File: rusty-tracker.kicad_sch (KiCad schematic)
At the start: 176 parts, among them J1 SIM8051-6-0-14-01-X, J2 USB_C_Receptacle_USB2.0, J3 NFC, J4 tag-connect-swd, J5 Battery Connector, J6 Conn_01x01, J7 Conn_01x01, Q1 RUM002N02T2L, Q2 RUM002N02T2L, Q3 RUM002N02T2L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

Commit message: Order sent to JLCPCB
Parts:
- J3: footprint Connector_JST:JST_SH_SM02B-SRSS-TB_1x02-1MP_P1.00mm_Horizontal -> Connector_FFC-FPC:TE_0-1734839-5_1x05-1MP_P0.5mm_Horizontal; symbol Connector_Generic_MountingPin:Conn_01x02_MountingPin -> Connector_Generic_MountingPin:Conn_01x05_MountingPin
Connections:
- net NFC1: now also J3.2 (Pin_2); no longer J3.1 (Pin_1)
- net NFC2: now also J3.4 (Pin_4); no longer J3.2 (Pin_2)
- no-connect marks 57 -> 60
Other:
- moved on the sheet: C17, C20
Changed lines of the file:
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@@
   (junction (at 190.5 177.8) (diameter 0) (color 0 0 0 0)
   )
-  (junction (at 382.27 121.92) (diameter 0) (color 0 0 0 0)
+  (junction (at 383.54 119.38) (diameter 0) (color 0 0 0 0)
   )
   (junction (at 280.67 72.39) (diameter 0) (color 0 0 0 0)
@@
   (junction (at 173.99 165.1) (diameter 0) (color 0 0 0 0)
   )
-  (junction (at 382.27 124.46) (diameter 0) (color 0 0 0 0)
+  (junction (at 383.54 124.46) (diameter 0) (color 0 0 0 0)
   )
   (junction (at 173.99 222.25) (diameter 0) (color 0 0 0 0)
@@
   (no_connect (at 107.95 91.44))
   (no_connect (at 353.06 165.1))
+  (no_connect (at 386.08 121.92))
   (no_connect (at 142.24 252.73))
   (no_connect (at 50.8 227.33))
@@
   (no_connect (at 107.95 60.96))
   (no_connect (at 142.24 250.19))
+  (no_connect (at 386.08 116.84))
   (no_connect (at 68.58 227.33))
   (no_connect (at 287.02 205.74))
@@
   (no_connect (at 77.47 227.33))
   (no_connect (at 107.95 58.42))
+  (no_connect (at 386.08 127))
   (no_connect (at 64.77 62.23))
   (no_connect (at 24.13 227.33))
@@
     (stroke (width 0) (type default))
   )
-  (wire (pts (xy 382.27 124.46) (xy 382.27 127))
+  (wire (pts (xy 383.54 124.46) (xy 383.54 127))
     (stroke (width 0) (type default))
   )
@@
     (stroke (width 0) (type default))
   )
-  (wire (pts (xy 382.27 119.38) (xy 382.27 121.92))
+  (wire (pts (xy 383.54 116.84) (xy 383.54 119.38))
     (stroke (width 0) (type default))
   )
@@
     (stroke (width 0) (type default))
   )
-  (wire (pts (xy 378.46 124.46) (xy 382.27 124.46))
+  (wire (pts (xy 379.73 124.46) (xy 383.54 124.46))
     (stroke (width 0) (type default))
   )
@@
     (stroke (width 0) (type default))
   )
-  (wire (pts (xy 378.46 121.92) (xy 382.27 121.92))
+  (wire (pts (xy 379.73 119.38) (xy 383.54 119.38))
     (stroke (width 0) (type default))
   )
@@
     (stroke (width 0.3) (type default))
   )
-  (wire (pts (xy 382.27 121.92) (xy 384.81 121.92))
+  (wire (pts (xy 383.54 119.38) (xy 386.08 119.38))
     (stroke (width 0) (type default))
   )
@@
     (stroke (width 0) (type default))
   )
-  (wire (pts (xy 382.27 124.46) (xy 384.81 124.46))
+  (wire (pts (xy 383.54 124.46) (xy 386.08 124.46))
     (stroke (width 0) (type default))
   )
@@
     (effects (font (size 1.27 1.27)) (justify left bottom))
   )
-  (label "NFC1" (at 378.46 124.46 180) (fields_autoplaced)
+  (label "NFC1" (at 379.73 124.46 180) (fields_autoplaced)
     (effects (font (size 1.27 1.27)) (justify right bottom))
   )
@@
     (effects (font (size 1.27 1.27)) (justify right bottom))
   )
-  (label "NFC2" (at 378.46 121.92 180) (fields_autoplaced)
+  (label "NFC2" (at 379.73 119.38 180) (fields_autoplaced)
     (effects (font (size 1.27 1.27)) (justify right bottom))
   )
@@
     )
   )
-  (symbol (lib_id "power:GND") (at 382.27 114.3 0) (mirror x) (unit 1)
+  (symbol (lib_id "power:GND") (at 383.54 111.76 0) (mirror x) (unit 1)
     (in_bom yes) (on_board yes) (dnp no)
-    (property "Reference" "#PWR055" (at 382.27 107.95 0)
+    (property "Reference" "#PWR055" (at 383.54 105.41 0)
       (effects (font (size 1.27 1.27)) hide)
     )
-    (property "Value" "GND" (at 382.397 111.0488 90)
+    (property "Value" "GND" (at 383.667 108.5088 90)
       (effects (font (size 1.27 1.27)) (justify right) hide)
     )
-    (property "Footprint" "" (at 382.27 114.3 0)
+    (property "Footprint" "" (at 383.54 111.76 0)
       (effects (font (size 1.27 1.27)))
     )
-    (property "Datasheet" "" (at 382.27 114.3 0)
+    (property "Datasheet" "" (at 383.54 111.76 0)
       (effects (font (size 1.27 1.27)))
     )
@@
     )
   )
-  (symbol (lib_id "Device:C_Small") (at 382.27 129.54 0) (mirror y) (unit 1)
-    (in_bom yes) (on_board yes) (dnp no)
-    (property "Reference" "C20" (at 384.6068 130.7084 0)
-      (effects (font (size 1.27 1.27)) (justify right))
+  (symbol (lib_id "Device:C_Small") (at 383.54 129.54 0) (mirror y) (unit 1)
+    (in_bom yes) (on_board yes) (dnp no) (fields_autoplaced)
+    (property "Reference" "C20" (at 381 128.9113 0)
+      (effects (font (size 1.27 1.27)) (justify left))
     )
-    (property "Value" "DNP" (at 384.6068 128.397 0)
-      (effects (font (size 1.27 1.27)) (justify right))
+    (property "Value" "DNP" (at 381 131.4513 0)
+      (effects (font (size 1.27 1.27)) (justify left))
     )
-    (property "Footprint" "passive:C_0402" (at 382.27 129.54 0)
+    (property "Footprint" "passive:C_0402" (at 383.54 129.54 0)
       (effects (font (size 1.27 1.27)) hide)
     )
-    (property "Datasheet" "" (at 382.27 129.54 0)
+    (property "Datasheet" "" (at 383.54 129.54 0)
       (effects (font (size 1.27 1.27)))
     )
-    (property "Tolerance" "" (at 382.27 129.54 0)
+    (property "Tolerance" "" (at 383.54 129.54 0)
       (effects (font (size 1.524 1.524)) hide)
     )
-    (property "Manufacturer" "" (at 528.32 309.88 0)
+    (property "Manufacturer" "" (at 529.59 309.88 0)
       (effects (font (size 1.524 1.524)) hide)
     )
-    (property "MFPN" "" (at 382.27 129.54 0)
+    (property "MFPN" "" (at 383.54 129.54 0)
       (effects (font (size 1.27 1.27)) hide)
     )
-    (property "Comment" "C0G,50V" (at 382.27 129.54 0)
+    (property "Comment" "C0G,50V" (at 383.54 129.54 0)
       (effects (font (size 1.27 1.27)) hide)
     )
@@
     )
   )
-  (symbol (lib_id "power:GND") (at 382.27 132.08 0) (mirror y) (unit 1)
+  (symbol (lib_id "power:GND") (at 383.54 132.08 0) (mirror y) (unit 1)
     (in_bom yes) (on_board yes) (dnp no)
-    (property "Reference" "#PWR059" (at 382.27 138.43 0)
+    (property "Reference" "#PWR059" (at 383.54 138.43 0)
       (effects (font (size 1.27 1.27)) hide)
     )
-    (property "Value" "GND" (at 382.143 135.3312 90)
+    (property "Value" "GND" (at 383.413 135.3312 90)
       (effects (font (size 1.27 1.27)) (justify right) hide)
     )
-    (property "Footprint" "" (at 382.27 132.08 0)
+    (property "Footprint" "" (at 383.54 132.08 0)
       (effects (font (size 1.27 1.27)))
     )
-    (property "Datasheet" "" (at 382.27 132.08 0)
+    (property "Datasheet" "" (at 383.54 132.08 0)
       (effects (font (size 1.27 1.27)))
     )
@@
     )
   )
-  (symbol (lib_id "power:GND") (at 389.89 116.84 180) (unit 1)
+  (symbol (lib_id "power:GND") (at 391.16 111.76 180) (unit 1)
     (in_bom yes) (on_board yes) (dnp no) (fields_autoplaced)
-    (property "Reference" "#PWR061" (at 389.89 110.49 0)
+    (property "Reference" "#PWR061" (at 391.16 105.41 0)
       (effects (font (size 1.27 1.27)) hide)
     )
-    (property "Value" "GND" (at 389.763 113.5888 90)
+    (property "Value" "GND" (at 391.033 108.5088 90)
       (effects (font (size 1.27 1.27)) (justify right) hide)
     )
-    (property "Footprint" "" (at 389.89 116.84 0)
+    (property "Footprint" "" (at 391.16 111.76 0)
       (effects (font (size 1.27 1.27)) hide)
     )
-    (property "Datasheet" "" (at 389.89 116.84 0)
+    (property "Datasheet" "" (at 391.16 111.76 0)
       (effects (font (size 1.27 1.27)) hide)
     )
@@
     )
   )
-  (symbol (lib_id "Device:C_Small") (at 382.27 116.84 0) (mirror x) (unit 1)
-    (in_bom yes) (on_board yes) (dnp no)
-    (property "Reference" "C17" (at 379.9332 115.6716 0)
+  (symbol (lib_id "Device:C_Small") (at 383.54 114.3 0) (mirror x) (unit 1)
+    (in_bom yes) (on_board yes) (dnp no) (fields_autoplaced)
+    (property "Reference" "C17" (at 381 113.6586 0)
       (effects (font (size 1.27 1.27)) (justify right))
     )
-    (property "Value" "DNP" (at 379.9332 117.983 0)
+    (property "Value" "DNP" (at 381 116.1986 0)
       (effects (font (size 1.27 1.27)) (justify right))
     )
-    (property "Footprint" "passive:C_0402" (at 382.27 116.84 0)
+    (property "Footprint" "passive:C_0402" (at 383.54 114.3 0)
       (effects (font (size 1.27 1.27)) hide)
     )
-    (property "Datasheet" "" (at 382.27 116.84 0)
+    (property "Datasheet" "" (at 383.54 114.3 0)
       (effects (font (size 1.27 1.27)))
     )
-    (property "Tolerance" "" (at 382.27 116.84 0)
+    (property "Tolerance" "" (at 383.54 114.3 0)
       (effects (font (size 1.524 1.524)) hide)
     )
-    (property "Manufacturer" "" (at 236.22 -63.5 0)
+    (property "Manufacturer" "" (at 237.49 -66.04 0)
       (effects (font (size 1.524 1.524)) hide)
     )
-    (property "MFPN" "" (at 382.27 116.84 0)
+    (property "MFPN" "" (at 383.54 114.3 0)
       (effects (font (size 1.27 1.27)) hide)
     )
-    (property "Comment" "C0G,50V" (at 382.27 116.84 0)
+    (property "Comment" "C0G,50V" (at 383.54 114.3 0)
       (effects (font (size 1.27 1.27)) hide)
     )
@@
     )
   )
-  (symbol (lib_id "Connector_Generic_MountingPin:Conn_01x02_MountingPin") (at 389.89 124.46 0) (mirror x) (unit 1)
+  (symbol (lib_id "Connector_Generic_MountingPin:Conn_01x05_MountingPin") (at 391.16 121.92 0) (mirror x) (unit 1)
     (in_bom yes) (on_board yes) (dnp no) (fields_autoplaced)
-    (property "Reference" "J3" (at 392.43 121.5643 0)
+    (property "Reference" "J3" (at 393.7 119.0243 0)
       (effects (font (size 1.27 1.27)) (justify left))
     )
-    (property "Value" "NFC" (at 392.43 124.1043 0)
+    (property "Value" "NFC" (at 393.7 121.5643 0)
       (effects (font (size 1.27 1.27)) (justify left))
     )
-    (property "Footprint" "Connector_JST:JST_SH_SM02B-SRSS-TB_1x02-1MP_P1.00mm_Horizontal" (at 389.89 124.46 0)
+    (property "Footprint" "Connector_FFC-FPC:TE_0-1734839-5_1x05-1MP_P0.5mm_Horizontal" (at 391.16 121.92 0)
       (effects (font (size 1.27 1.27)) hide)
     )
-    (property "Datasheet" "~" (at 389.89 124.46 0)
+    (property "Datasheet" "~" (at 391.16 121.92 0)
       (effects (font (size 1.27 1.27)) hide)
     )
-    (property "MFPN" "SM02B-SRSS-TB(LF)(SN)" (at 389.89 124.46 0)
+    (property "MFPN" "SM02B-SRSS-TB(LF)(SN)" (at 391.16 121.92 0)
       (effects (font (size 1.27 1.27)) hide)
     )
     (pin "1")
     (pin "2")
+    (pin "3")
+    (pin "4")
+    (pin "5")
     (pin "MP")
     (instances

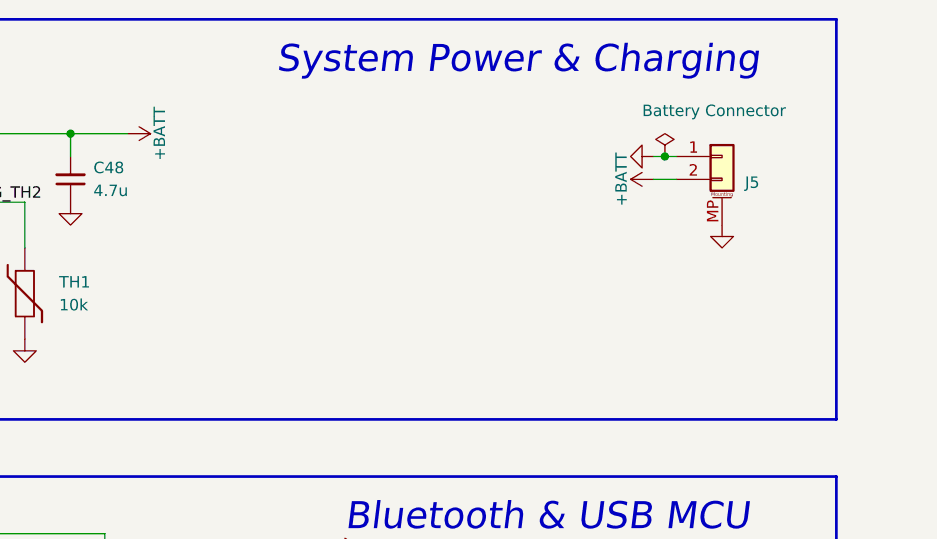
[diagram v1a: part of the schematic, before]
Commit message: Add an exported schematic so people don't need to download and check
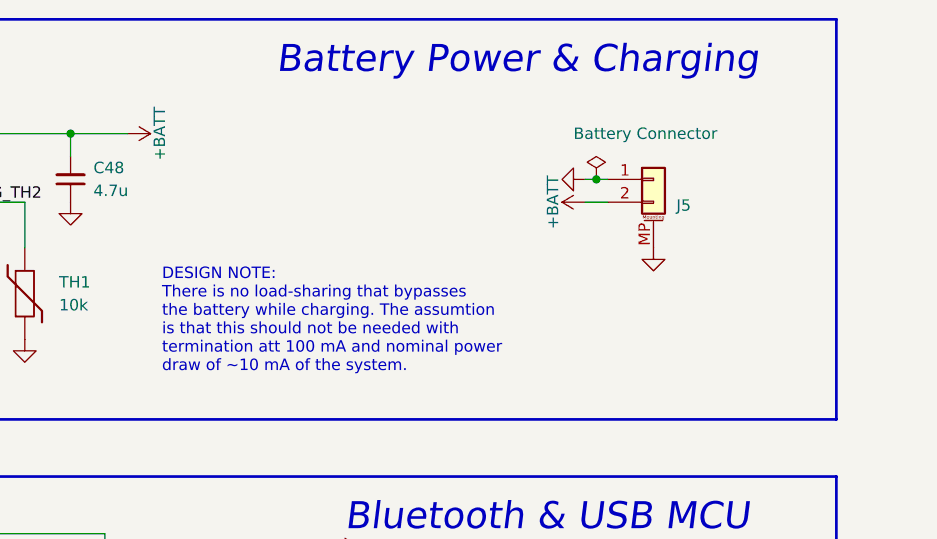
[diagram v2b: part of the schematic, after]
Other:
- note added: "Battery Power & Charging"
- note added: "DESIGN NOTE: There is no load-sharing that bypasses the battery while charging. The assumtion is that this should not be needed with termination att 100 mA and nominal power draw of ~10 mA of the system."
- note removed: "System Power & Charging"
- moved on the sheet: J5
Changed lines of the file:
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@@
   (junction (at 58.42 133.35) (diameter 0) (color 0 0 0 0)
   )
-  (junction (at 382.27 30.48) (diameter 0) (color 0 0 0 0)
+  (junction (at 374.65 33.02) (diameter 0) (color 0 0 0 0)
   )
   (junction (at 381 226.06) (diameter 0) (color 0 0 0 0)
@@
     (stroke (width 0.3) (type default))
   )
-  (wire (pts (xy 382.27 30.48) (xy 383.54 30.48))
+  (wire (pts (xy 374.65 33.02) (xy 375.92 33.02))
     (stroke (width 0) (type default))
   )
@@
     (stroke (width 0) (type default))
   )
-  (wire (pts (xy 381 33.02) (xy 383.54 33.02))
+  (wire (pts (xy 373.38 35.56) (xy 375.92 35.56))
     (stroke (width 0) (type default))
   )
@@
     (stroke (width 0) (type default))
   )
-  (wire (pts (xy 381 30.48) (xy 382.27 30.48))
+  (wire (pts (xy 373.38 33.02) (xy 374.65 33.02))
     (stroke (width 0) (type default))
   )
@@
     (effects (font (size 2 2) italic) (justify right bottom))
   )
-  (text "System Power & Charging" (at 339.09 21.59 0)
+  (text "Battery Power & Charging" (at 339.09 21.59 0)
     (effects (font (size 3 3) italic) (justify left bottom))
   )
@@
     (effects (font (size 2 2) italic) (justify right bottom))
   )
+  (text "DESIGN NOTE:\nThere is no load-sharing that bypasses \nthe battery while charging. The assumtion \nis that this should not be needed with \ntermination att 100 mA and nominal power \ndraw of ~10 mA of the system."
+    (at 326.39 54.61 0)
+    (effects (font (size 1.27 1.27)) (justify left bottom))
+  )
   (label "DEC4_6" (at 312.42 91.44 90) (fields_autoplaced)
     (effects (font (size 1.27 1.27)) (justify left bottom))
@@
     )
   )
-  (symbol (lib_id "power:PWR_FLAG") (at 382.27 30.48 0) (mirror y) (unit 1)
+  (symbol (lib_id "power:PWR_FLAG") (at 374.65 33.02 0) (mirror y) (unit 1)
     (in_bom yes) (on_board yes) (dnp no) (fields_autoplaced)
-    (property "Reference" "#FLG0102" (at 382.27 28.575 0)
+    (property "Reference" "#FLG0102" (at 374.65 31.115 0)
       (effects (font (size 1.27 1.27)) hide)
     )
-    (property "Value" "PWR_FLAG" (at 382.27 25.4 0)
+    (property "Value" "PWR_FLAG" (at 374.65 27.94 0)
       (effects (font (size 1.27 1.27)) hide)
     )
-    (property "Footprint" "" (at 382.27 30.48 0)
+    (property "Footprint" "" (at 374.65 33.02 0)
       (effects (font (size 1.27 1.27)) hide)
     )
-    (property "Datasheet" "~" (at 382.27 30.48 0)
+    (property "Datasheet" "~" (at 374.65 33.02 0)
       (effects (font (size 1.27 1.27)) hide)
     )
@@
     )
   )
-  (symbol (lib_id "power:GND") (at 381 30.48 270) (mirror x) (unit 1)
+  (symbol (lib_id "power:GND") (at 373.38 33.02 270) (mirror x) (unit 1)
     (in_bom yes) (on_board yes) (dnp no) (fields_autoplaced)
-    (property "Reference" "#PWR056" (at 374.65 30.48 0)
+    (property "Reference" "#PWR056" (at 367.03 33.02 0)
       (effects (font (size 1.27 1.27)) hide)
     )
-    (property "Value" "GND" (at 377.7488 30.353 90)
+    (property "Value" "GND" (at 370.1288 32.893 90)
       (effects (font (size 1.27 1.27)) (justify right) hide)
     )
-    (property "Footprint" "" (at 381 30.48 0)
+    (property "Footprint" "" (at 373.38 33.02 0)
       (effects (font (size 1.27 1.27)) hide)
     )
-    (property "Datasheet" "" (at 381 30.48 0)
+    (property "Datasheet" "" (at 373.38 33.02 0)
       (effects (font (size 1.27 1.27)) hide)
     )
@@
     )
   )
-  (symbol (lib_id "power:+BATT") (at 381 33.02 90) (mirror x) (unit 1)
+  (symbol (lib_id "power:+BATT") (at 373.38 35.56 90) (mirror x) (unit 1)
     (in_bom yes) (on_board yes) (dnp no) (fields_autoplaced)
-    (property "Reference" "#PWR0142" (at 384.81 33.02 0)
+    (property "Reference" "#PWR0142" (at 377.19 35.56 0)
       (effects (font (size 1.27 1.27)) hide)
     )
-    (property "Value" "+BATT" (at 377.444 33.02 0)
+    (property "Value" "+BATT" (at 369.824 35.56 0)
       (effects (font (size 1.27 1.27)))
     )
-    (property "Footprint" "" (at 381 33.02 0)
+    (property "Footprint" "" (at 373.38 35.56 0)
       (effects (font (size 1.27 1.27)) hide)
     )
-    (property "Datasheet" "" (at 381 33.02 0)
+    (property "Datasheet" "" (at 373.38 35.56 0)
       (effects (font (size 1.27 1.27)) hide)
     )
@@
     )
   )
-  (symbol (lib_id "Connector_Generic_MountingPin:Conn_01x02_MountingPin") (at 388.62 30.48 0) (unit 1)
+  (symbol (lib_id "Connector_Generic_MountingPin:Conn_01x02_MountingPin") (at 381 33.02 0) (unit 1)
     (in_bom yes) (on_board yes) (dnp no)
-    (property "Reference" "J5" (at 391.16 33.3757 0)
+    (property "Reference" "J5" (at 383.54 35.9157 0)
       (effects (font (size 1.27 1.27)) (justify left))
     )
-    (property "Value" "Battery Connector" (at 379.73 25.4 0)
+    (property "Value" "Battery Connector" (at 372.11 27.94 0)
       (effects (font (size 1.27 1.27)) (justify left))
     )
-    (property "Footprint" "Connector_JST:JST_SH_SM02B-SRSS-TB_1x02-1MP_P1.00mm_Horizontal" (at 388.62 30.48 0)
+    (property "Footprint" "Connector_JST:JST_SH_SM02B-SRSS-TB_1x02-1MP_P1.00mm_Horizontal" (at 381 33.02 0)
       (effects (font (size 1.27 1.27)) hide)
     )
-    (property "Datasheet" "~" (at 388.62 30.48 0)
+    (property "Datasheet" "~" (at 381 33.02 0)
       (effects (font (size 1.27 1.27)) hide)
     )
-    (property "MFPN" "SM02B-SRSS-TB(LF)(SN)" (at 388.62 30.48 0)
+    (property "MFPN" "SM02B-SRSS-TB(LF)(SN)" (at 381 33.02 0)
       (effects (font (size 1.27 1.27)) hide)
     )
@@
     )
   )
-  (symbol (lib_id "power:GND") (at 388.62 38.1 0) (mirror y) (unit 1)
+  (symbol (lib_id "power:GND") (at 381 40.64 0) (mirror y) (unit 1)
     (in_bom yes) (on_board yes) (dnp no) (fields_autoplaced)
-    (property "Reference" "#PWR057" (at 388.62 44.45 0)
+    (property "Reference" "#PWR057" (at 381 46.99 0)
       (effects (font (size 1.27 1.27)) hide)
     )
-    (property "Value" "GND" (at 388.493 41.3512 90)
+    (property "Value" "GND" (at 380.873 43.8912 90)
       (effects (font (size 1.27 1.27)) (justify right) hide)
     )
-    (property "Footprint" "" (at 388.62 38.1 0)
+    (property "Footprint" "" (at 381 40.64 0)
       (effects (font (size 1.27 1.27)) hide)
     )
-    (property "Datasheet" "" (at 388.62 38.1 0)
+    (property "Datasheet" "" (at 381 40.64 0)
       (effects (font (size 1.27 1.27)) hide)
     )
